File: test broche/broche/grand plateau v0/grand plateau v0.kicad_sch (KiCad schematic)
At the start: 64 parts

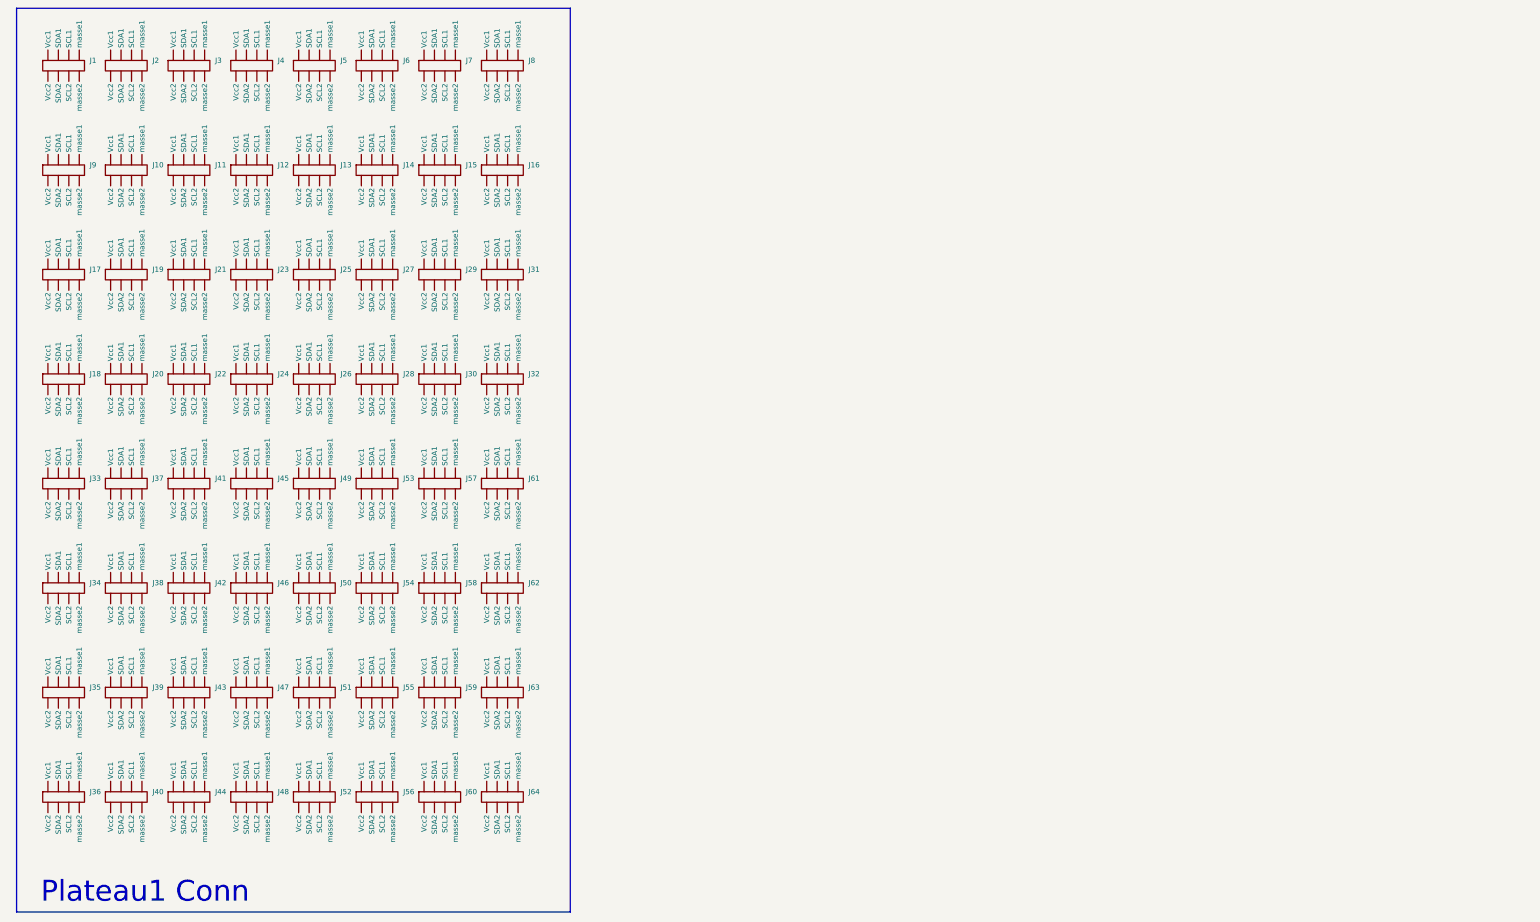
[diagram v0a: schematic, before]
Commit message: ajout de feuilles hiérarchiques
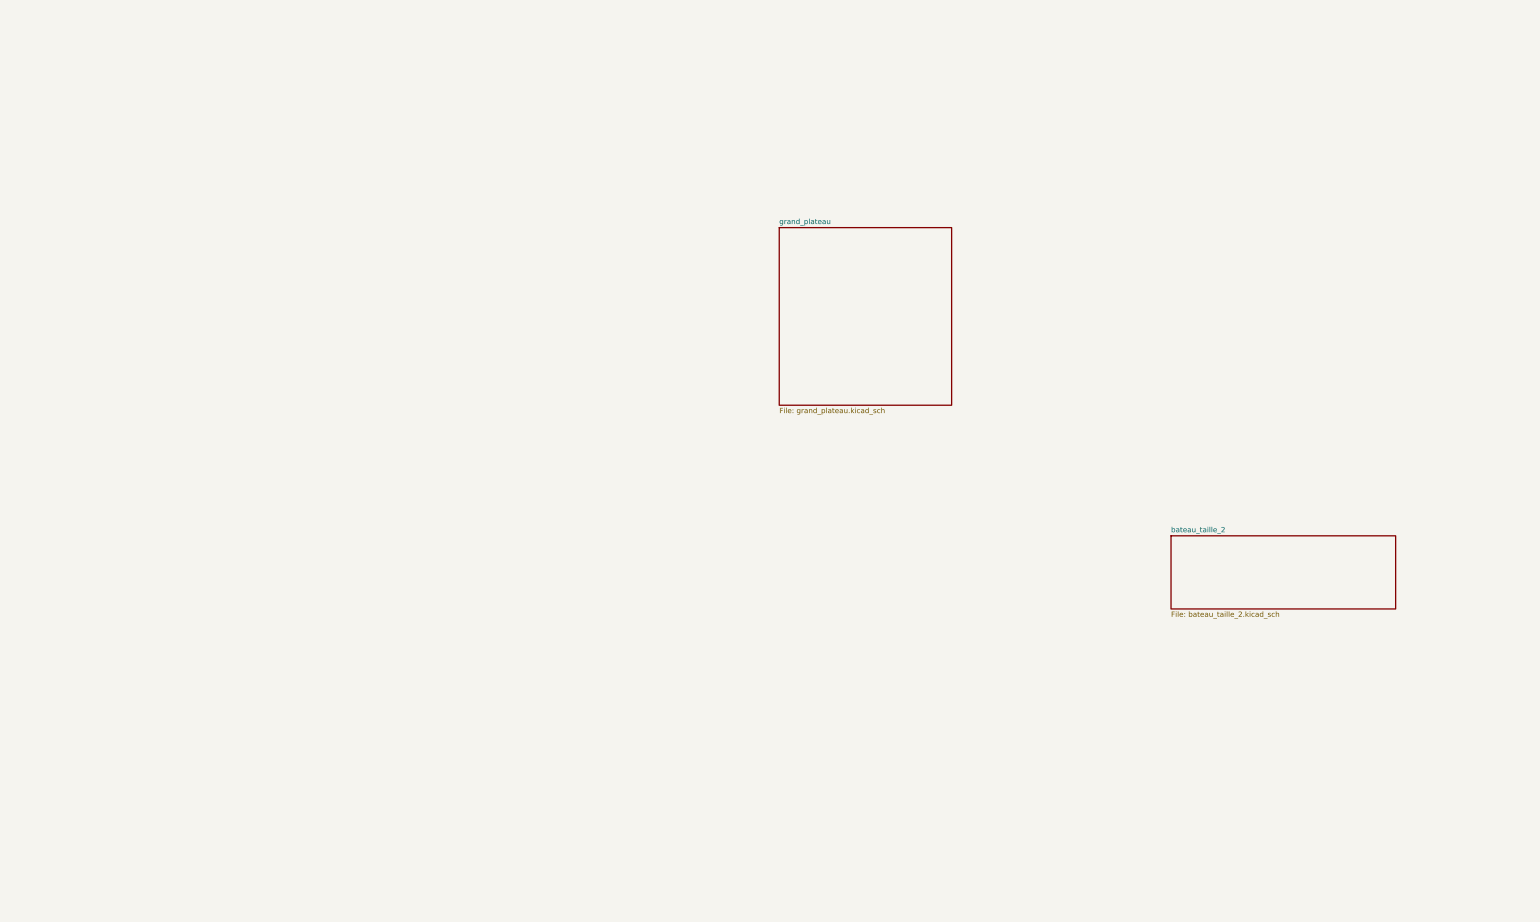
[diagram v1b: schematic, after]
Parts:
- removed J1, J10, J11, J12, J13, J14, J15, J16, J17, J18, J19, J2, J20, J21, J22, J23, J24, J25, J26, J27, J28, J29, J3, J30, J31, J32, J33, J34, J35, J36, J37, J38, J39, J4, J40, J41, J42, J43, J44, J45, J46, J47, J48, J49, J5, J50, J51, J52, J53, J54, J55, J56, J57, J58, J59, J6, J60, J61, J62, J63, J64, J7, J8, J9: ~, Mes_empreintes:Untitled, symbol Mes_symboles:Conn_rond_8_1
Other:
- added sheet bateau_taille_2 (bateau_taille_2.kicad_sch)
- added sheet grand_plateau (grand_plateau.kicad_sch)
- note removed: "Plateau1 Conn"

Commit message: bateaux
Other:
- added sheet bateau_taille_3 (bateau_taille_3.kicad_sch)
- added sheet bateau_taille_4 (bateau_taille_4.kicad_sch)
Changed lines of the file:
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@@
 	(paper "A3")
 	(sheet
-		(at 299.72 148.59)
+		(at 246.38 40.64)
+		(size 49.53 33.02)
+		(exclude_from_sim no)
+		(in_bom yes)
+		(on_board yes)
+		(dnp no)
+		(fields_autoplaced yes)
+		(stroke
+			(width 0.1524)
+			(type solid)
+		)
+		(fill
+			(color 0 0 0 0.0000)
+		)
+		(property "Sheetname" "bateau_taille_3"
+			(at 246.38 39.9284 0)
+			(effects
+				(font
+					(size 1.27 1.27)
+				)
+				(justify left bottom)
+			)
+		)
+		(property "Sheetfile" "bateau_taille_3.kicad_sch"
+			(at 246.38 74.2446 0)
+			(effects
+				(font
+					(size 1.27 1.27)
+				)
+				(justify left top)
+			)
+		)
+		(instances
+			(project "grand plateau v0"
+				(path "/7a85495e-2bfc-48e4-8ed7-0a3f11b4bc2f"
+					(page "4")
+				)
+			)
+		)
+	)
+	(sheet
+		(at 170.18 49.53)
 		(size 54.61 17.78)
 		(exclude_from_sim no)
@@
 		)
 		(property "Sheetname" "bateau_taille_2"
-			(at 299.72 147.8784 0)
+			(at 170.18 48.8184 0)
 			(effects
 				(font
@@
 		)
 		(property "Sheetfile" "bateau_taille_2.kicad_sch"
-			(at 299.72 166.9546 0)
+			(at 170.18 67.8946 0)
 			(effects
 				(font
@@
 	)
 	(sheet
-		(at 204.47 73.66)
+		(at 73.66 39.37)
 		(size 41.91 43.18)
 		(exclude_from_sim no)
@@
 		)
 		(property "Sheetname" "grand_plateau"
-			(at 204.47 72.9484 0)
+			(at 73.66 38.6584 0)
 			(effects
 				(font
@@
 		)
 		(property "Sheetfile" "grand_plateau.kicad_sch"
-			(at 204.47 117.4246 0)
+			(at 73.66 83.1346 0)
 			(effects
 				(font
@@
 				)
 			)
+		)
+	)
+	(sheet
+		(at 326.39 36.83)
+		(size 60.96 41.91)
+		(exclude_from_sim no)
+		(in_bom yes)
+		(on_board yes)
+		(dnp no)
+		(fields_autoplaced yes)
+		(stroke
+			(width 0.1524)
+			(type solid)
+		)
+		(fill
+			(color 0 0 0 0.0000)
+		)
+		(property "Sheetname" "bateau_taille_4"
+			(at 326.39 36.1184 0)
+			(effects
+				(font
+					(size 1.27 1.27)
+				)
+				(justify left bottom)
+			)
+		)
+		(property "Sheetfile" "bateau_taille_4.kicad_sch"
+			(at 326.39 79.3246 0)
+			(effects
+				(font
+					(size 1.27 1.27)
+				)
+				(justify left top)
+			)
+		)
+		(instances
+			(project "grand plateau v0"
+				(path "/7a85495e-2bfc-48e4-8ed7-0a3f11b4bc2f"
+					(page "5")
+				)
+			)
